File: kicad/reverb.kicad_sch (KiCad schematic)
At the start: 20 parts, among them IC1 TL072CP

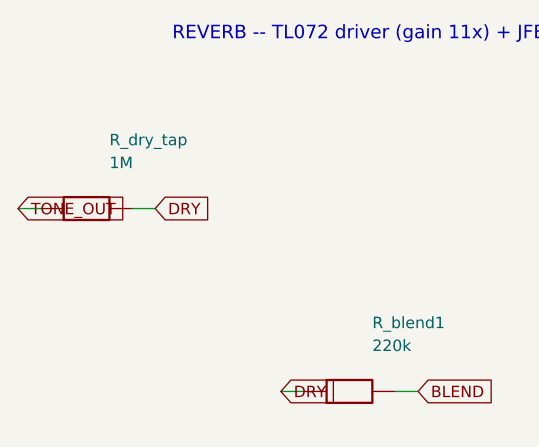
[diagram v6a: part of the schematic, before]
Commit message: Roast pass (2026-06-16): fix missing mains fuse, correct 18W->~12W spec, +more
Adversarial review (docs/roast-2026-06-16.md), every finding verified by math or
file. Fixes applied:

R1 (SAFETY, was missing): added a MAINS PRIMARY fuse. The only fuse was a 1A on
   the secondary DC rail, which doesn't protect against a primary/transformer/
   bridge fault. Added T800mA/250V (120V; ~T400mA at 230V) to BOM + Part 1 safety
   + Part 3.
R2 (spec error I propagated last pass): "18 W into 8 ohm" is physically
   unreachable on a 33.5 V single rail -- needs 17.0 V peak, only 16.75 V exists.
   Real ceiling ~12 W clean (17.5 W absolute). Corrected Part 1 sec.3, Part 5
   thermal, and the component-availability-audit current/transformer numbers
   (which I'd built on the bad 18 W: ~30 VA min, not ~50 VA "match").
R3: the reverb dry/wet mixer is broken as drawn -- 1M series in the dry path vs
   220k wet made it ~all-wet, into an unbuffered high-Z blend node. Rebalanced
   R_dry_tap 1M->220k and flagged loudly that the inter-effect chain needs a real
   buffered summing stage before fab.
R4: marked the orphaned Wiring_Edge_Array_35 footprint (advertised, never placed)
   as unused/reference.
R5-R8 (documented): F1 sits in the C_main inrush path (prefer AC-secondary);
   shared VBIAS can bleed tremolo into reverb; "SPICE-verified" oversells (the
   macromodel is rail-less -> no single-supply headroom/clipping check); and the
   CHANGELOG was incoherent (floating section, all-same-date) -> consolidated.

Verified after regen: sch erc 0, full DRC unchanged (164), demo DRC 0, SPICE
exit 0, BOM CSV clean.

https://claude.ai/code/session_01PkrfUi9tvZfLvudJ7h23qD
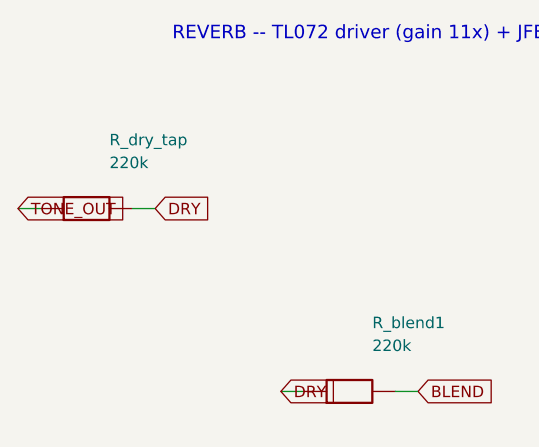
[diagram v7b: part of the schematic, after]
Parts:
- R_dry_tap: value 1M -> 220k
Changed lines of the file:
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@@
     (pin "8")
     (pin "4")
-    (instances (project "cambridge_reverb" (path "/8d697993-52de-477e-bbde-a154689b24ff" (reference "IC1") (unit 1))))
+    (instances (project "cambridge_reverb" (path "/5ab7b92f-edb2-4b60-9354-5e291575d58a" (reference "IC1") (unit 1))))
   )
   (wire (pts (xy 179.07 111.76) (xy 176.52999999999997 111.76)) (stroke (width 0) (type default)))
@@
     (pin "1")
     (pin "2")
-    (instances (project "cambridge_reverb" (path "/8d697993-52de-477e-bbde-a154689b24ff" (reference "C_drvin") (unit 1))))
+    (instances (project "cambridge_reverb" (path "/5ab7b92f-edb2-4b60-9354-5e291575d58a" (reference "C_drvin") (unit 1))))
   )
   (wire (pts (xy 115.57 201.93) (xy 113.03 201.93)) (stroke (width 0) (type default)))
@@
     (pin "1")
     (pin "2")
-    (instances (project "cambridge_reverb" (path "/8d697993-52de-477e-bbde-a154689b24ff" (reference "R_drvbias") (unit 1))))
+    (instances (project "cambridge_reverb" (path "/5ab7b92f-edb2-4b60-9354-5e291575d58a" (reference "R_drvbias") (unit 1))))
   )
   (wire (pts (xy 151.13 201.93) (xy 148.59 201.93)) (stroke (width 0) (type default)))
@@
     (pin "1")
     (pin "2")
-    (instances (project "cambridge_reverb" (path "/8d697993-52de-477e-bbde-a154689b24ff" (reference "R_drv1") (unit 1))))
+    (instances (project "cambridge_reverb" (path "/5ab7b92f-edb2-4b60-9354-5e291575d58a" (reference "R_drv1") (unit 1))))
   )
   (wire (pts (xy 226.06 91.44) (xy 223.52 91.44)) (stroke (width 0) (type default)))
@@
     (pin "1")
     (pin "2")
-    (instances (project "cambridge_reverb" (path "/8d697993-52de-477e-bbde-a154689b24ff" (reference "R_drv2") (unit 1))))
+    (instances (project "cambridge_reverb" (path "/5ab7b92f-edb2-4b60-9354-5e291575d58a" (reference "R_drv2") (unit 1))))
   )
   (wire (pts (xy 226.06 147.32) (xy 223.52 147.32)) (stroke (width 0) (type default)))
@@
     (pin "1")
     (pin "2")
-    (instances (project "cambridge_reverb" (path "/8d697993-52de-477e-bbde-a154689b24ff" (reference "C_rev1") (unit 1))))
+    (instances (project "cambridge_reverb" (path "/5ab7b92f-edb2-4b60-9354-5e291575d58a" (reference "C_rev1") (unit 1))))
   )
   (wire (pts (xy 236.22 116.84) (xy 233.68 116.84)) (stroke (width 0) (type default)))
@@
     (pin "1")
     (pin "2")
-    (instances (project "cambridge_reverb" (path "/8d697993-52de-477e-bbde-a154689b24ff" (reference "R_drv3") (unit 1))))
+    (instances (project "cambridge_reverb" (path "/5ab7b92f-edb2-4b60-9354-5e291575d58a" (reference "R_drv3") (unit 1))))
   )
   (wire (pts (xy 271.78 116.84) (xy 269.24 116.84)) (stroke (width 0) (type default)))
@@
     (pin "3")
     (pin "4")
-    (instances (project "cambridge_reverb" (path "/8d697993-52de-477e-bbde-a154689b24ff" (reference "REV1") (unit 1))))
+    (instances (project "cambridge_reverb" (path "/5ab7b92f-edb2-4b60-9354-5e291575d58a" (reference "REV1") (unit 1))))
   )
   (wire (pts (xy 307.34000000000003 121.92) (xy 304.8 121.92)) (stroke (width 0) (type default)))
@@
     (pin "1")
     (pin "2")
-    (instances (project "cambridge_reverb" (path "/8d697993-52de-477e-bbde-a154689b24ff" (reference "C_rev2") (unit 1))))
+    (instances (project "cambridge_reverb" (path "/5ab7b92f-edb2-4b60-9354-5e291575d58a" (reference "C_rev2") (unit 1))))
   )
   (wire (pts (xy 135.89 156.20999999999998) (xy 133.35 156.20999999999998)) (stroke (width 0) (type default)))
@@
     (pin "1")
     (pin "3")
-    (instances (project "cambridge_reverb" (path "/8d697993-52de-477e-bbde-a154689b24ff" (reference "Q_rec") (unit 1))))
+    (instances (project "cambridge_reverb" (path "/5ab7b92f-edb2-4b60-9354-5e291575d58a" (reference "Q_rec") (unit 1))))
   )
   (wire (pts (xy 184.14999999999998 176.52999999999997) (xy 181.60999999999999 176.52999999999997)) (stroke (width 0) (type default)))
@@
     (pin "1")
     (pin "2")
-    (instances (project "cambridge_reverb" (path "/8d697993-52de-477e-bbde-a154689b24ff" (reference "R_rec_bias") (unit 1))))
+    (instances (project "cambridge_reverb" (path "/5ab7b92f-edb2-4b60-9354-5e291575d58a" (reference "R_rec_bias") (unit 1))))
   )
   (wire (pts (xy 135.89 186.69) (xy 133.35 186.69)) (stroke (width 0) (type default)))
@@
     (pin "1")
     (pin "2")
-    (instances (project "cambridge_reverb" (path "/8d697993-52de-477e-bbde-a154689b24ff" (reference "R_rec1") (unit 1))))
+    (instances (project "cambridge_reverb" (path "/5ab7b92f-edb2-4b60-9354-5e291575d58a" (reference "R_rec1") (unit 1))))
   )
   (wire (pts (xy 186.69 152.39999999999998) (xy 184.14999999999998 152.39999999999998)) (stroke (width 0) (type default)))
@@
     (pin "1")
     (pin "2")
-    (instances (project "cambridge_reverb" (path "/8d697993-52de-477e-bbde-a154689b24ff" (reference "R_rec2") (unit 1))))
+    (instances (project "cambridge_reverb" (path "/5ab7b92f-edb2-4b60-9354-5e291575d58a" (reference "R_rec2") (unit 1))))
   )
   (wire (pts (xy 186.69 207.01) (xy 184.14999999999998 207.01)) (stroke (width 0) (type default)))
@@
     (pin "1")
     (pin "2")
-    (instances (project "cambridge_reverb" (path "/8d697993-52de-477e-bbde-a154689b24ff" (reference "C_rec_byp") (unit 1))))
+    (instances (project "cambridge_reverb" (path "/5ab7b92f-edb2-4b60-9354-5e291575d58a" (reference "C_rec_byp") (unit 1))))
   )
   (wire (pts (xy 226.06 207.01) (xy 223.52 207.01)) (stroke (width 0) (type default)))
@@
     (pin "1")
     (pin "2")
-    (instances (project "cambridge_reverb" (path "/8d697993-52de-477e-bbde-a154689b24ff" (reference "C_rev4") (unit 1))))
+    (instances (project "cambridge_reverb" (path "/5ab7b92f-edb2-4b60-9354-5e291575d58a" (reference "C_rev4") (unit 1))))
   )
   (wire (pts (xy 226.06 176.52999999999997) (xy 223.52 176.52999999999997)) (stroke (width 0) (type default)))
@@
     (pin "3")
     (pin "2")
-    (instances (project "cambridge_reverb" (path "/8d697993-52de-477e-bbde-a154689b24ff" (reference "POT_REV") (unit 1))))
+    (instances (project "cambridge_reverb" (path "/5ab7b92f-edb2-4b60-9354-5e291575d58a" (reference "POT_REV") (unit 1))))
   )
   (wire (pts (xy 275.59 186.69) (xy 273.04999999999995 186.69)) (stroke (width 0) (type default)))
@@
     (pin "1")
     (pin "2")
-    (instances (project "cambridge_reverb" (path "/8d697993-52de-477e-bbde-a154689b24ff" (reference "R_blend1") (unit 1))))
+    (instances (project "cambridge_reverb" (path "/5ab7b92f-edb2-4b60-9354-5e291575d58a" (reference "R_blend1") (unit 1))))
   )
   (wire (pts (xy 135.89 96.52) (xy 133.35 96.52)) (stroke (width 0) (type default)))
@@
     (pin "1")
     (pin "2")
-    (instances (project "cambridge_reverb" (path "/8d697993-52de-477e-bbde-a154689b24ff" (reference "R_blend2") (unit 1))))
+    (instances (project "cambridge_reverb" (path "/5ab7b92f-edb2-4b60-9354-5e291575d58a" (reference "R_blend2") (unit 1))))
   )
   (wire (pts (xy 135.89 127.0) (xy 133.35 127.0)) (stroke (width 0) (type default)))
@@
     (in_bom yes) (on_board yes) (dnp no)
     (property "Reference" "R_dry_tap" (at 114.30000000000001 68.57999999999998 0) (effects (font (size 1.27 1.27)) (justify left)))
-    (property "Value" "1M" (at 114.30000000000001 71.11999999999999 0) (effects (font (size 1.27 1.27)) (justify left)))
+    (property "Value" "220k" (at 114.30000000000001 71.11999999999999 0) (effects (font (size 1.27 1.27)) (justify left)))
     (property "Footprint" "Resistor_THT:R_Axial_DIN0207_L6.3mm_D2.5mm_P5.08mm_Vertical" (at 111.76 76.19999999999999 0) (effects (font (size 1.27 1.27)) hide))
     (pin "1")
     (pin "2")
-    (instances (project "cambridge_reverb" (path "/8d697993-52de-477e-bbde-a154689b24ff" (reference "R_dry_tap") (unit 1))))
+    (instances (project "cambridge_reverb" (path "/5ab7b92f-edb2-4b60-9354-5e291575d58a" (reference "R_dry_tap") (unit 1))))
   )
   (wire (pts (xy 106.68 76.19999999999999) (xy 104.14 76.19999999999999)) (stroke (width 0) (type default)))
@@
     (pin "1")
     (pin "2")
-    (instances (project "cambridge_reverb" (path "/8d697993-52de-477e-bbde-a154689b24ff" (reference "R_fs_rev") (unit 1))))
+    (instances (project "cambridge_reverb" (path "/5ab7b92f-edb2-4b60-9354-5e291575d58a" (reference "R_fs_rev") (unit 1))))
   )
   (wire (pts (xy 106.68 207.01) (xy 104.14 207.01)) (stroke (width 0) (type default)))

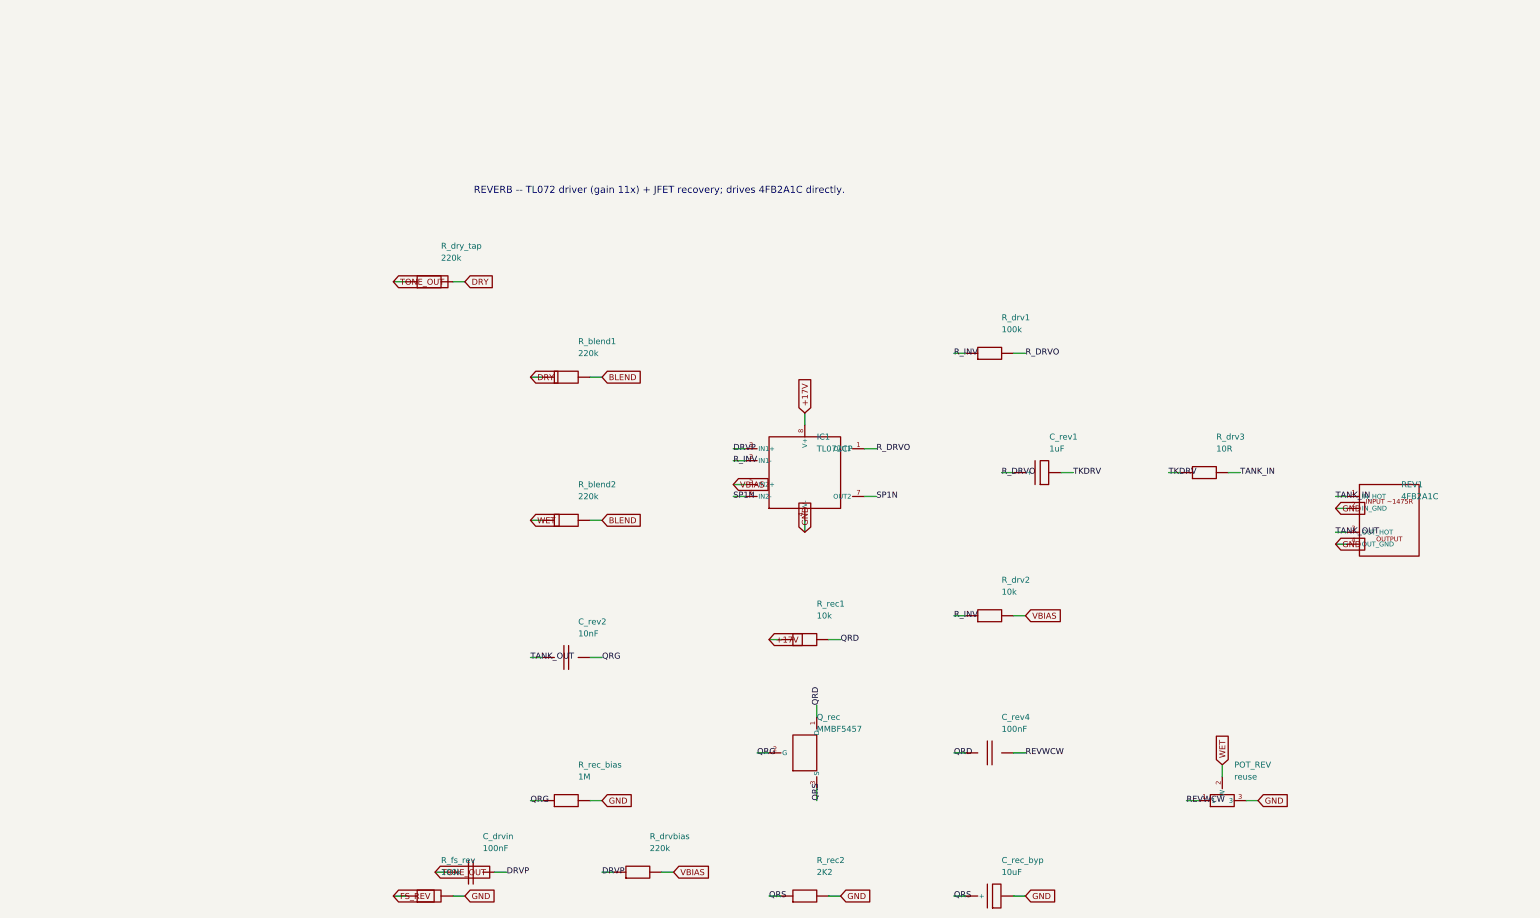
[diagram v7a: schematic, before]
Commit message: Redesign effects chain: active reverb summer + output buffer + split bias
Resolves roast R3 (broken passive mixer) and R6 (shared VBIAS bleed), using the
two spare TL072 halves and verifying with a rail-aware SPICE model.

- Reverb wet/dry mix is now an ACTIVE inverting summer on IC1-B (dry always on,
  wet via POT_REV, unity each, low-Z out about VBIAS_R). Removed the broken
  passive R_dry_tap/R_blend1/R_blend2 (1M dry series made it ~all-wet into an
  unbuffered 110k node).
- IC2-B repurposed as the post-MRB OUTPUT BUFFER driving PA_IN (removed the
  unbuffered R_painput 1M and a dead C_trem_out/R_trem_pass branch).
- VBIAS split into independent VBIAS_R (reverb) and VBIAS_T (tremolo) dividers
  (100k/100k + 47uF each) -> the LFO can no longer modulate the reverb reference.

Verification: new models/opamp_rail.sub clamps the output to the rails (unlike
opamp1p.sub), and spice/tran_reverb_mixer.cir confirms on a single +17V supply:
mid-rail bias 8.50 V, unity (0.0 dB) sum, clips at 15.5/1.5 V -> +-7 V headroom
(~24 dB over a 0.42 V program peak). This is the large-signal/headroom check the
rail-less model could not do (roast R7).

ERC 0; demo DRC 0; full board regenerated (106 footprints); run_all.sh exit 0;
BOM + roast doc + SCHEMATIC-BUILD + spice/README + CHANGELOG updated.

https://claude.ai/code/session_01PkrfUi9tvZfLvudJ7h23qD
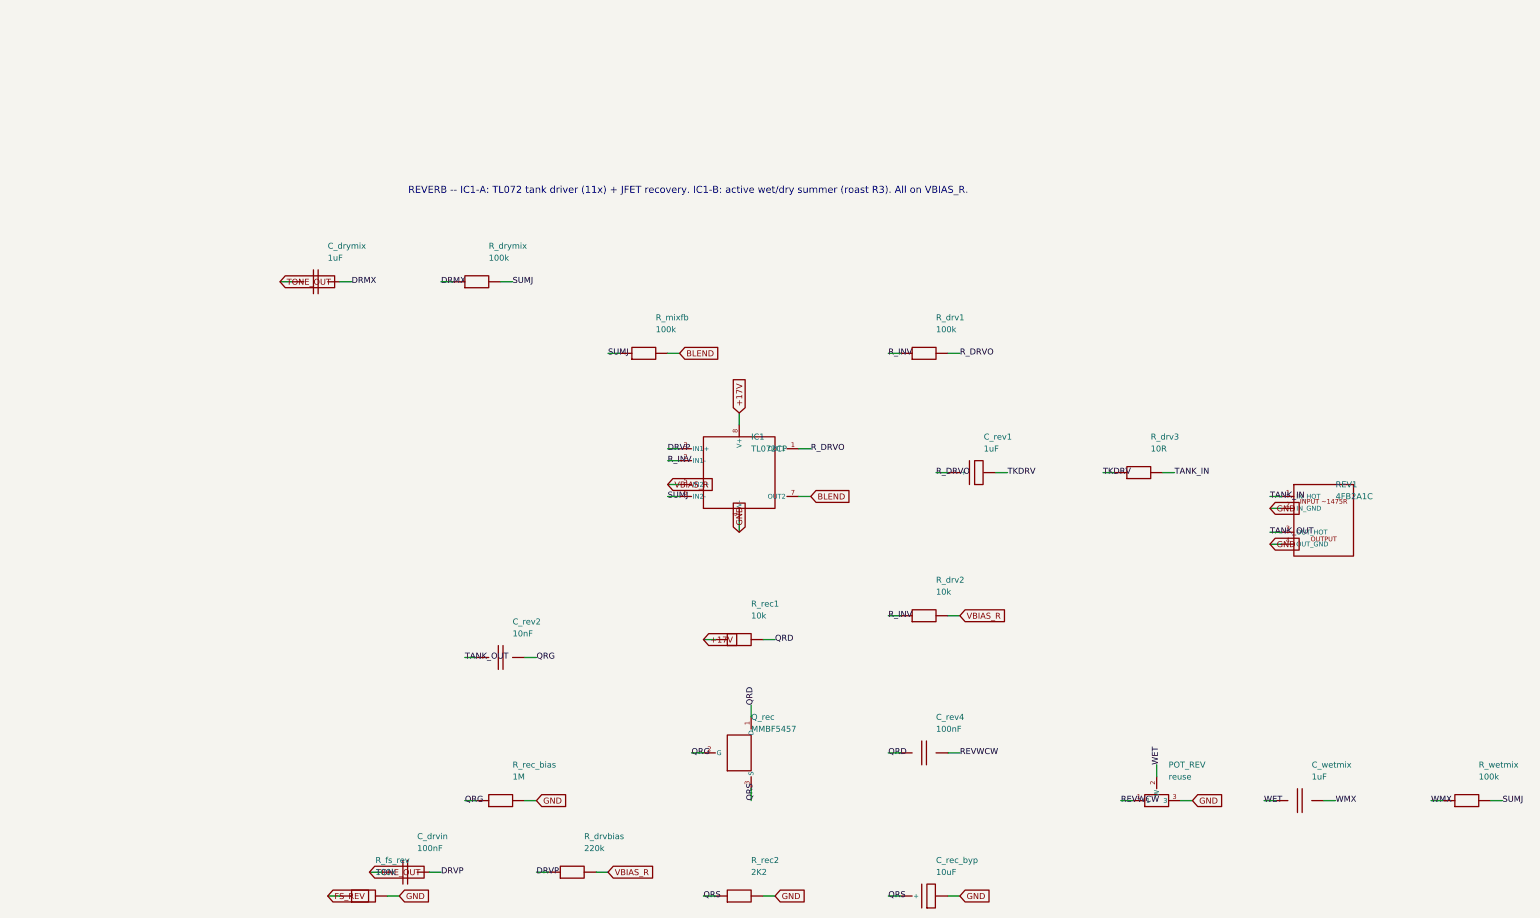
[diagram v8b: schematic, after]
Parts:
- removed R_blend1, R_blend2, R_dry_tap: 220k, Resistor_THT:R_Axial_DIN0207_L6.3mm_D2.5mm_P5.08mm_Vertical, symbol cr_primitives:R
- added C_drymix, C_wetmix: 1uF, Capacitor_THT:C_Disc_D7.5mm_W2.5mm_P5.00mm, symbol cr_primitives:C
- added R_drymix, R_mixfb, R_wetmix: 100k, Resistor_THT:R_Axial_DIN0207_L6.3mm_D2.5mm_P5.08mm_Vertical, symbol cr_primitives:R
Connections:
- net BLEND: now also IC1.7 (OUT2), R_mixfb.2
- net TONE_OUT: now also C_drymix.1
- net WET: now also C_wetmix.1
- net SP1N renamed SUMJ
- net SUMJ: now also R_drymix.2, R_mixfb.1, R_wetmix.2; no longer IC1.7 (OUT2)
- net VBIAS renamed VBIAS_R
- new net DRMX: C_drymix.2, R_drymix.1
- new net WMX: C_wetmix.2, R_wetmix.1
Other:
- note added: "REVERB -- IC1-A: TL072 tank driver (11x) + JFET recovery. IC1-B: active wet/dry summer (roast R3). All on VBIAS_R."
- note removed: "REVERB -- TL072 driver (gain 11x) + JFET recovery; drives 4FB2A1C directly."
